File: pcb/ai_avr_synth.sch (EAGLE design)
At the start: 45 parts, among them IC1 ATMEGA328P-PDIP, J1 1X02ST, J2 1X06, J3 1X08, J4 1X08, J5 MIDIJACK, J6 STEREOJACKSJ1-3555NG, U1 MC7805, U2 TLC2262, U3 6N138

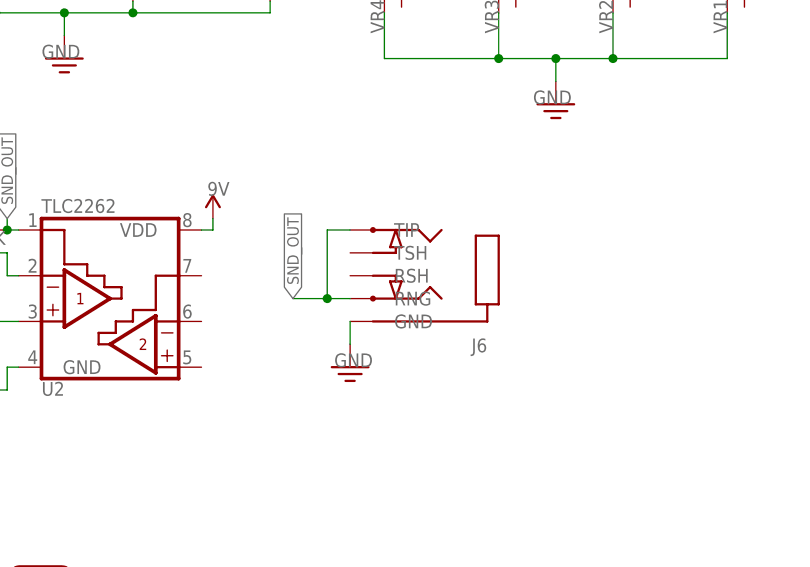
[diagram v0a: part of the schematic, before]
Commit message: changes to schematic fonts, and audiojack pad names
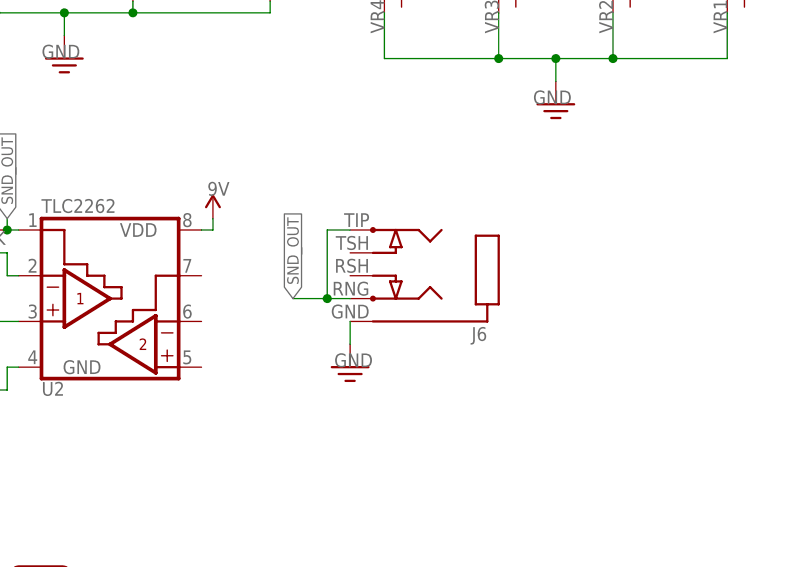
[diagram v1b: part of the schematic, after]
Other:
- moved on the sheet: J6

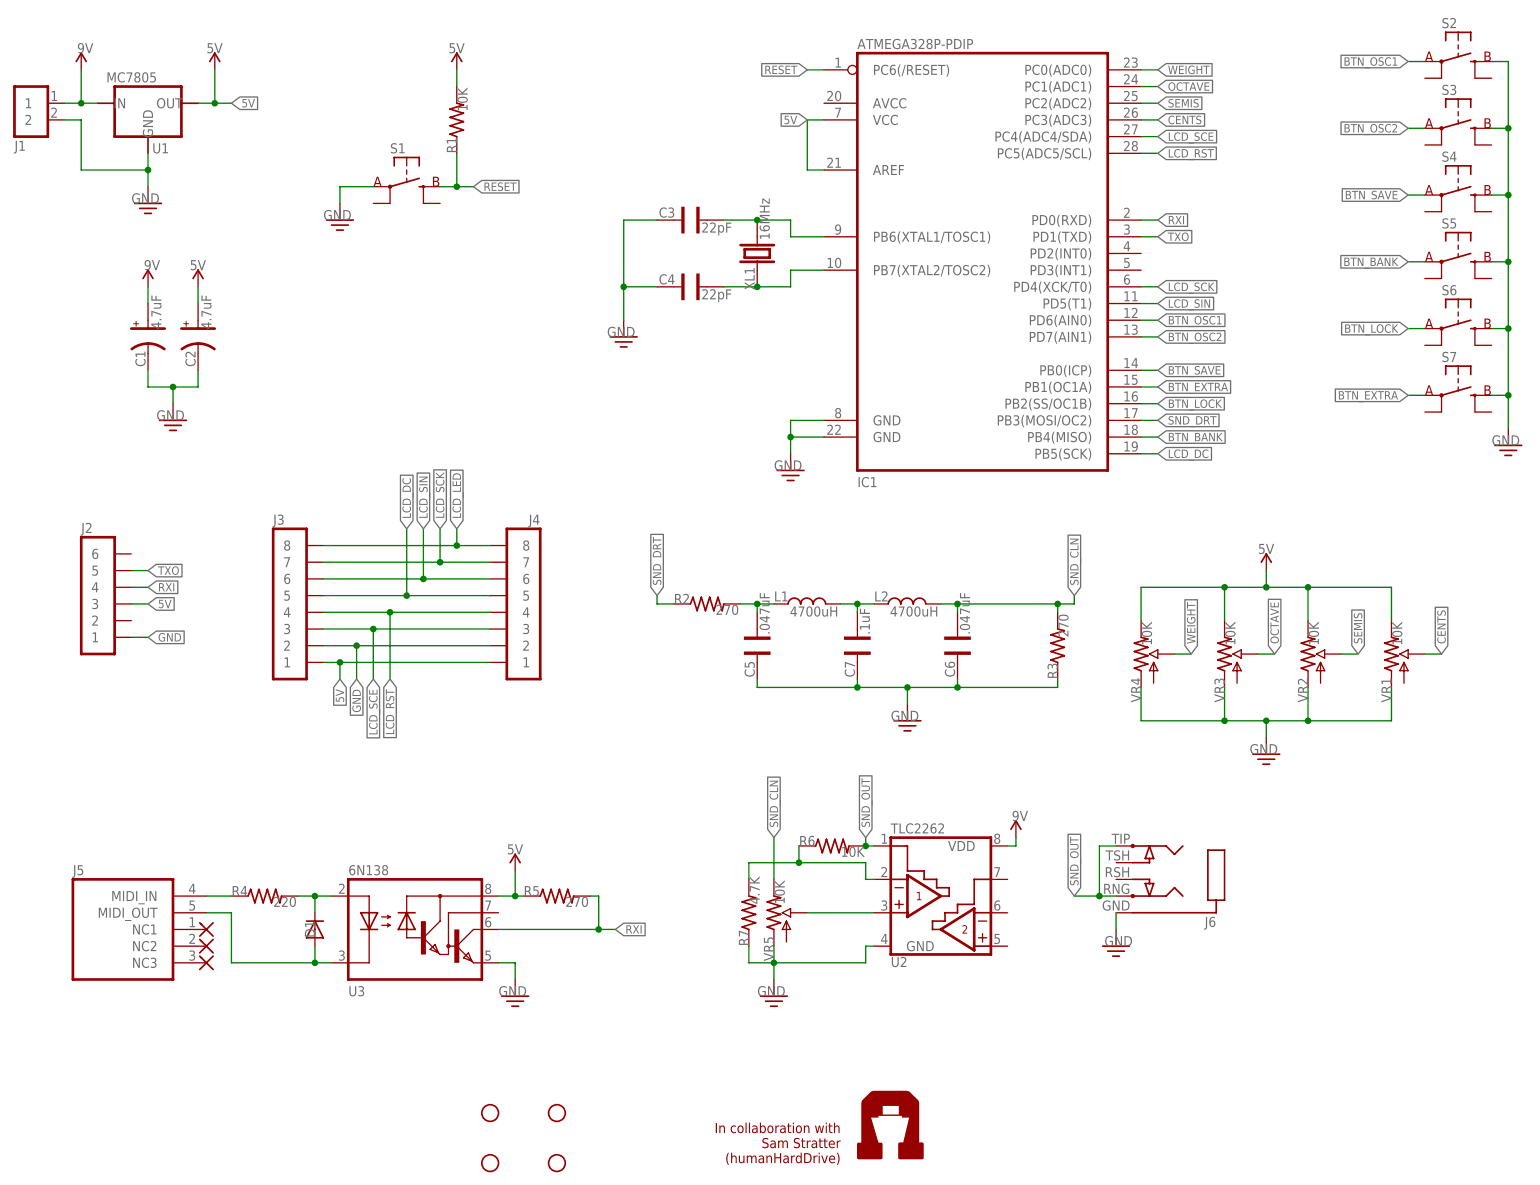
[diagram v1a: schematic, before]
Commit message: Updated components to use the latest libraries.  Had to redo a few traces (nothing major)
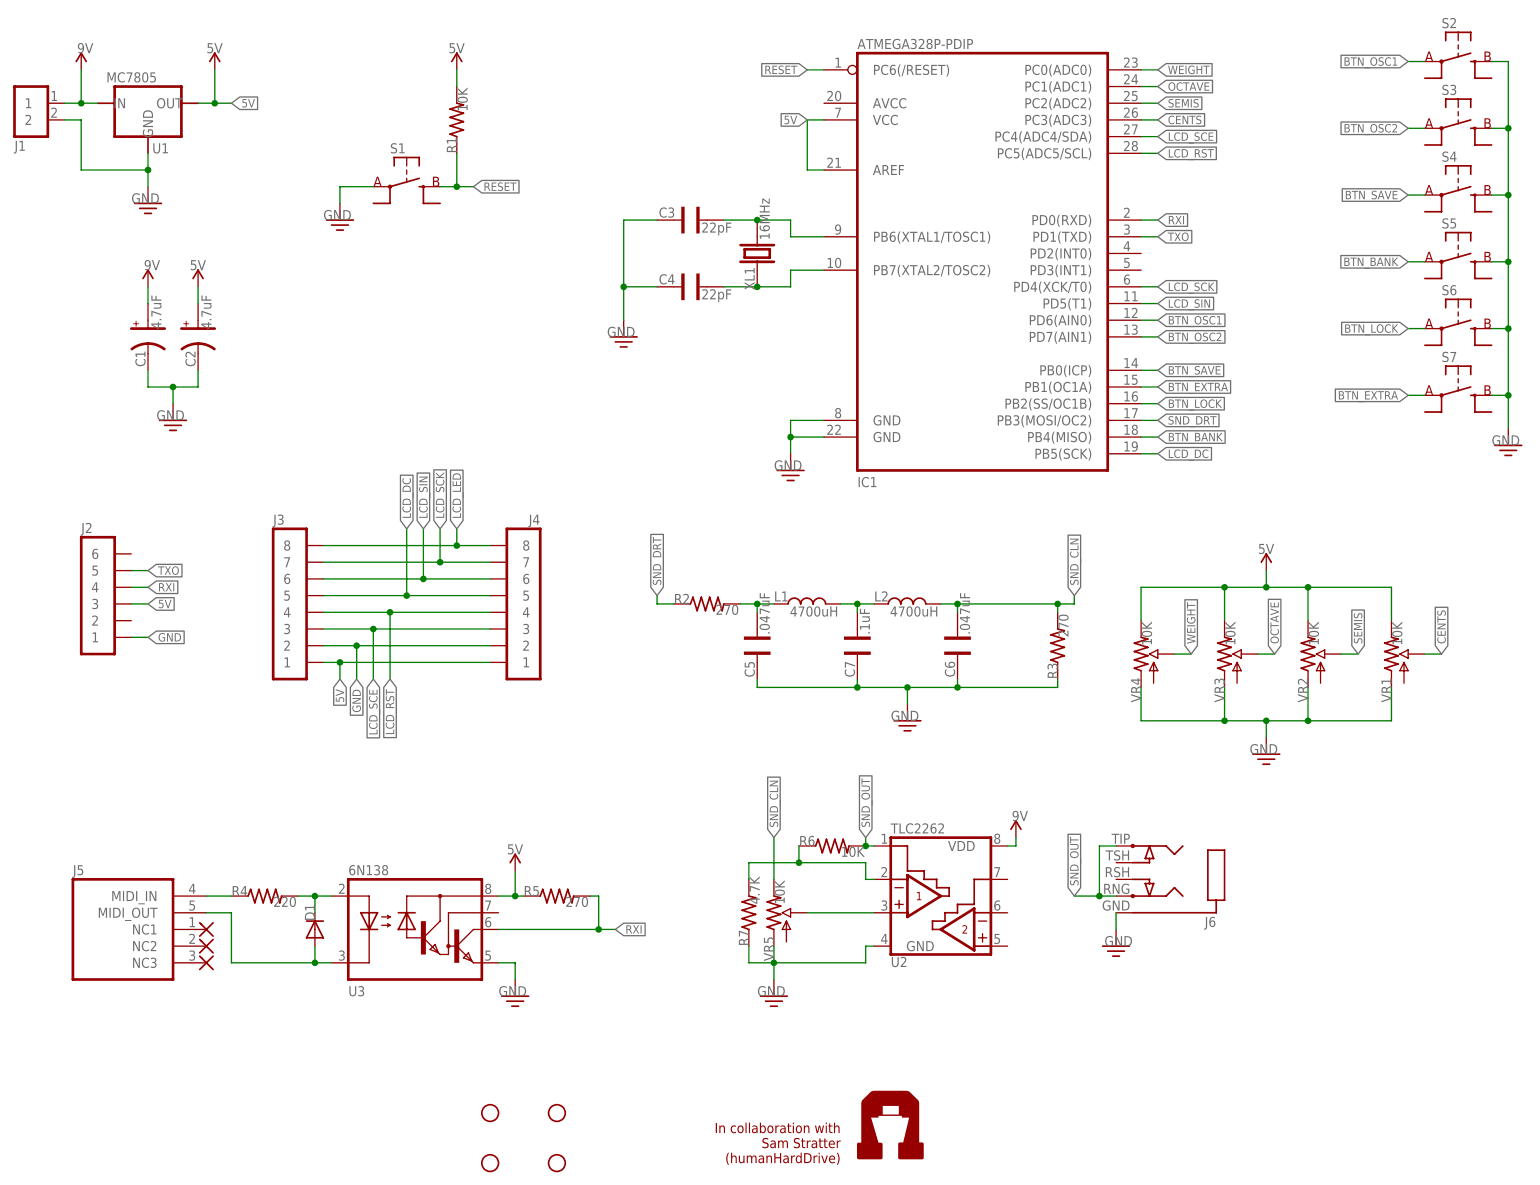
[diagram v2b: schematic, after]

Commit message: New version with modifications discussed with @humanHardDrive
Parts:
- removed J6: STEREOJACKSJ1-3555NG, Ai_Connectors:STEREOJACKSJ1-3555NG
- added 3.5MM: STEREOJACKSJ1-351XNG, Ai_Connectors:STEREOJACKSJ1-351XNG
- added C8: 0.1uF, Ai_Passives:CAP025X050
- added D2: (no value), Ai_DiscreteSemis:DIODETH-1N914
- added ISP: 2X03, Ai_Connectors:2X03
- added S8: SW-SPDTTH, Ai_Electromechanical:SW-SPDTTH
- added VR6: 10K, Ai_Passives:POT05X05
- C3, C4: device Ai_Passives:CAP055X070 -> Ai_Passives:CAP025X050
- C7: value .1uF -> 0.1uF
- D1: value DIODE1N914 -> (none); device Ai_DiscreteSemis:DIODE1N914 -> Ai_DiscreteSemis:DIODETH-1N914
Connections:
- new net N$2: C8.1, S2.B@1, S3.B@1, S4.B@1, S5.B@1, S6.B@1, S7.B@1
- new net N$5: J1.1, S8.COM
- new net N$7: D2.C, U1.IN
- net 5V: now also ISP.2, VR6.E
- net 9V: now also D2.A, S8.L2; no longer J1.1, U1.IN
- net BTN_BANK: now also ISP.1
- net GND: now also 3.5MM.GND, C8.2, ISP.6; no longer J6.GND, S2.B@1, S3.B@1, S4.B@1, S5.B@1, S6.B@1, S7.B@1
- net LCD_DC: now also ISP.3
- net LCD_LED: now also VR6.A
- net N$1: now also J5.MIDI_OUT; no longer J5.MIDI_IN
- net N$10: now also J5.MIDI_IN; no longer J5.MIDI_OUT
- net RESET: now also ISP.5, J2.6
- net SND_DRT: now also ISP.4
- net SND_OUT: now also 3.5MM.RNG, 3.5MM.TIP; no longer J6.RNG, J6.TIP
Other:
- moved on the sheet: D1, J1, R1, R4, S1, U1
